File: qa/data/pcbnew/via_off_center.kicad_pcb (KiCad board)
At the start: 4 copper layers, 87.8 x 45.7 mm, 6 parts

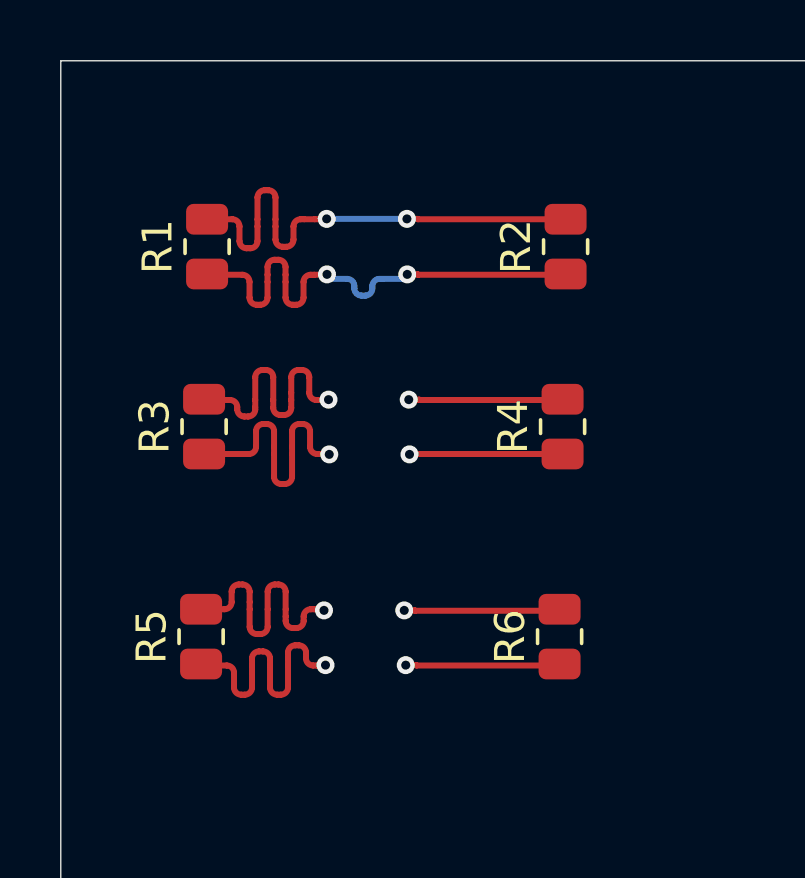
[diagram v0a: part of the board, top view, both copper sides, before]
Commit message: Update via_off_center test board with known trace lengths
Each net has a single point-to-point trace with a known length verified
manually and matching the tuning length. DRC constraints are tightened
per-net to validate that the calculated lengths match expected values.
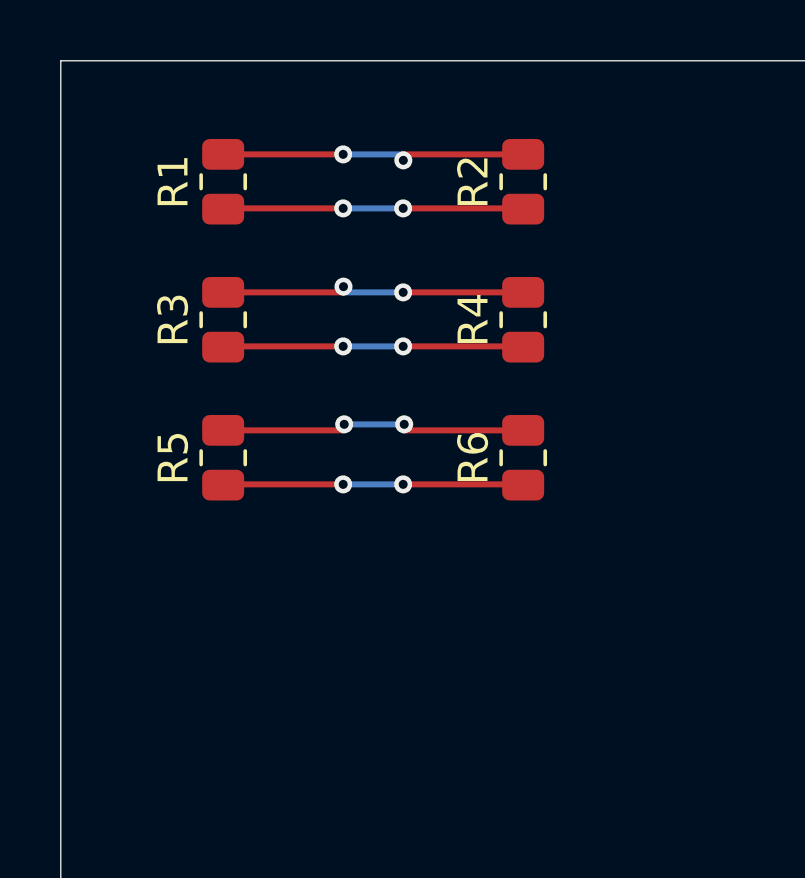
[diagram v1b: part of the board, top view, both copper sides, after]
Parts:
- moved R6 6.08 mm to (54.0, 48.1)
- moved R5 6.01 mm to (44.0, 48.1)
- moved R4 3.80 mm to (54.0, 43.5)
- moved R3 3.62 mm to (44.0, 43.5)
- moved R2 2.58 mm to (54.0, 38.9)
- moved R1 2.23 mm to (44.0, 38.9)
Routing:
- net /NON_CENTERED_B: track 19.5 -> 10.0 mm
- net /CENTERED_B: track 19.5 -> 10.0 mm
- net /CENTERED_C: track 17.1 -> 10.0 mm
- net /NON_CENTERED_C: track 17.0 -> 10.0 mm
- net /NON_CENTERED_A: track 16.8 -> 10.0 mm
- net /CENTERED_A: track 16.7 -> 10.0 mm
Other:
- board text removed: "R"
